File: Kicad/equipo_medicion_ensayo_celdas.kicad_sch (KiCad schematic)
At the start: 63 parts, among them J1 Conn_01x12, J3 Screw_Terminal_01x02, J4 Screw_Terminal_01x02, Q1 CSD17308Q3, Q2 CSD17308Q3, Q3 CSD17308Q3, Q4 CSD17308Q3, Q5 CSD17308Q3, Q6 2N2222A, Q7 TIP36C, U1 BQ24780SRUYR, U2 STM32WB55RGVx, U3 LM358

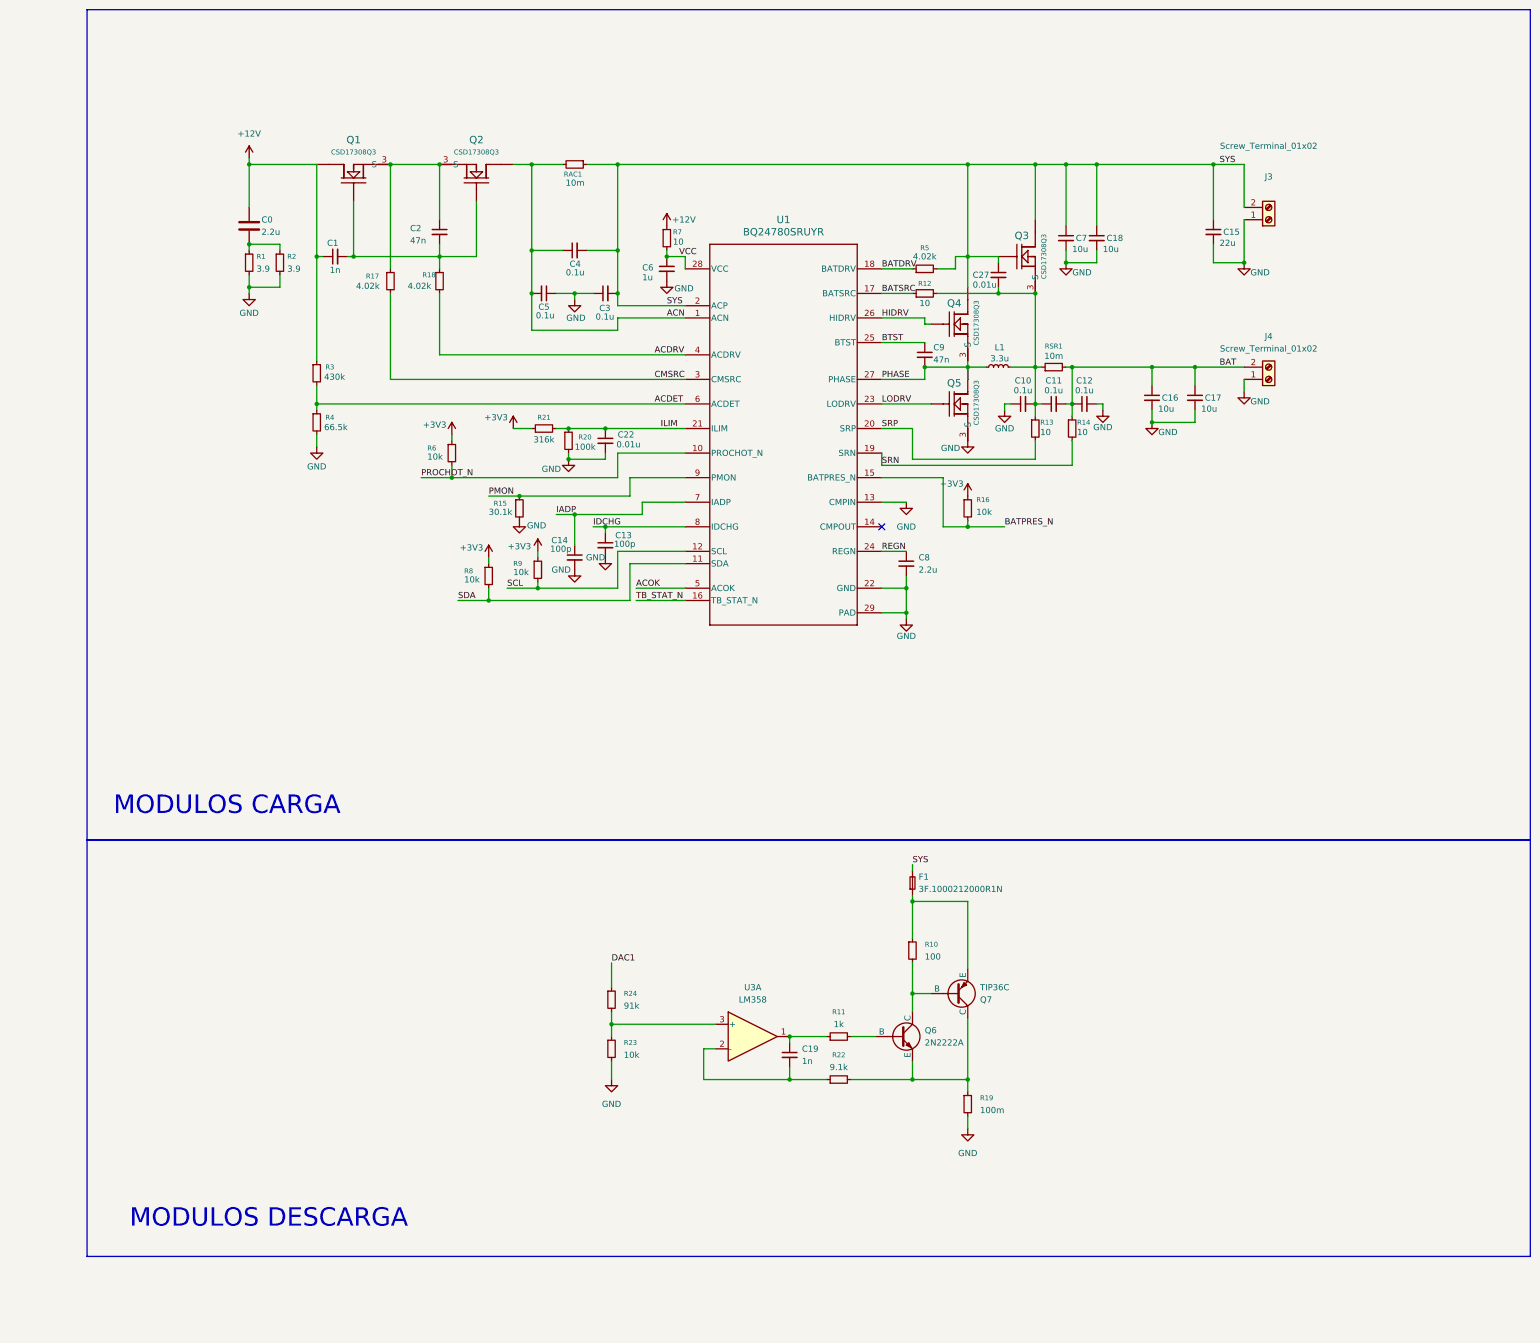
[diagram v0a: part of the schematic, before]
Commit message: Mejoras y arreglos en diseño de módulo carga/descarga/acir y fw de prueba.
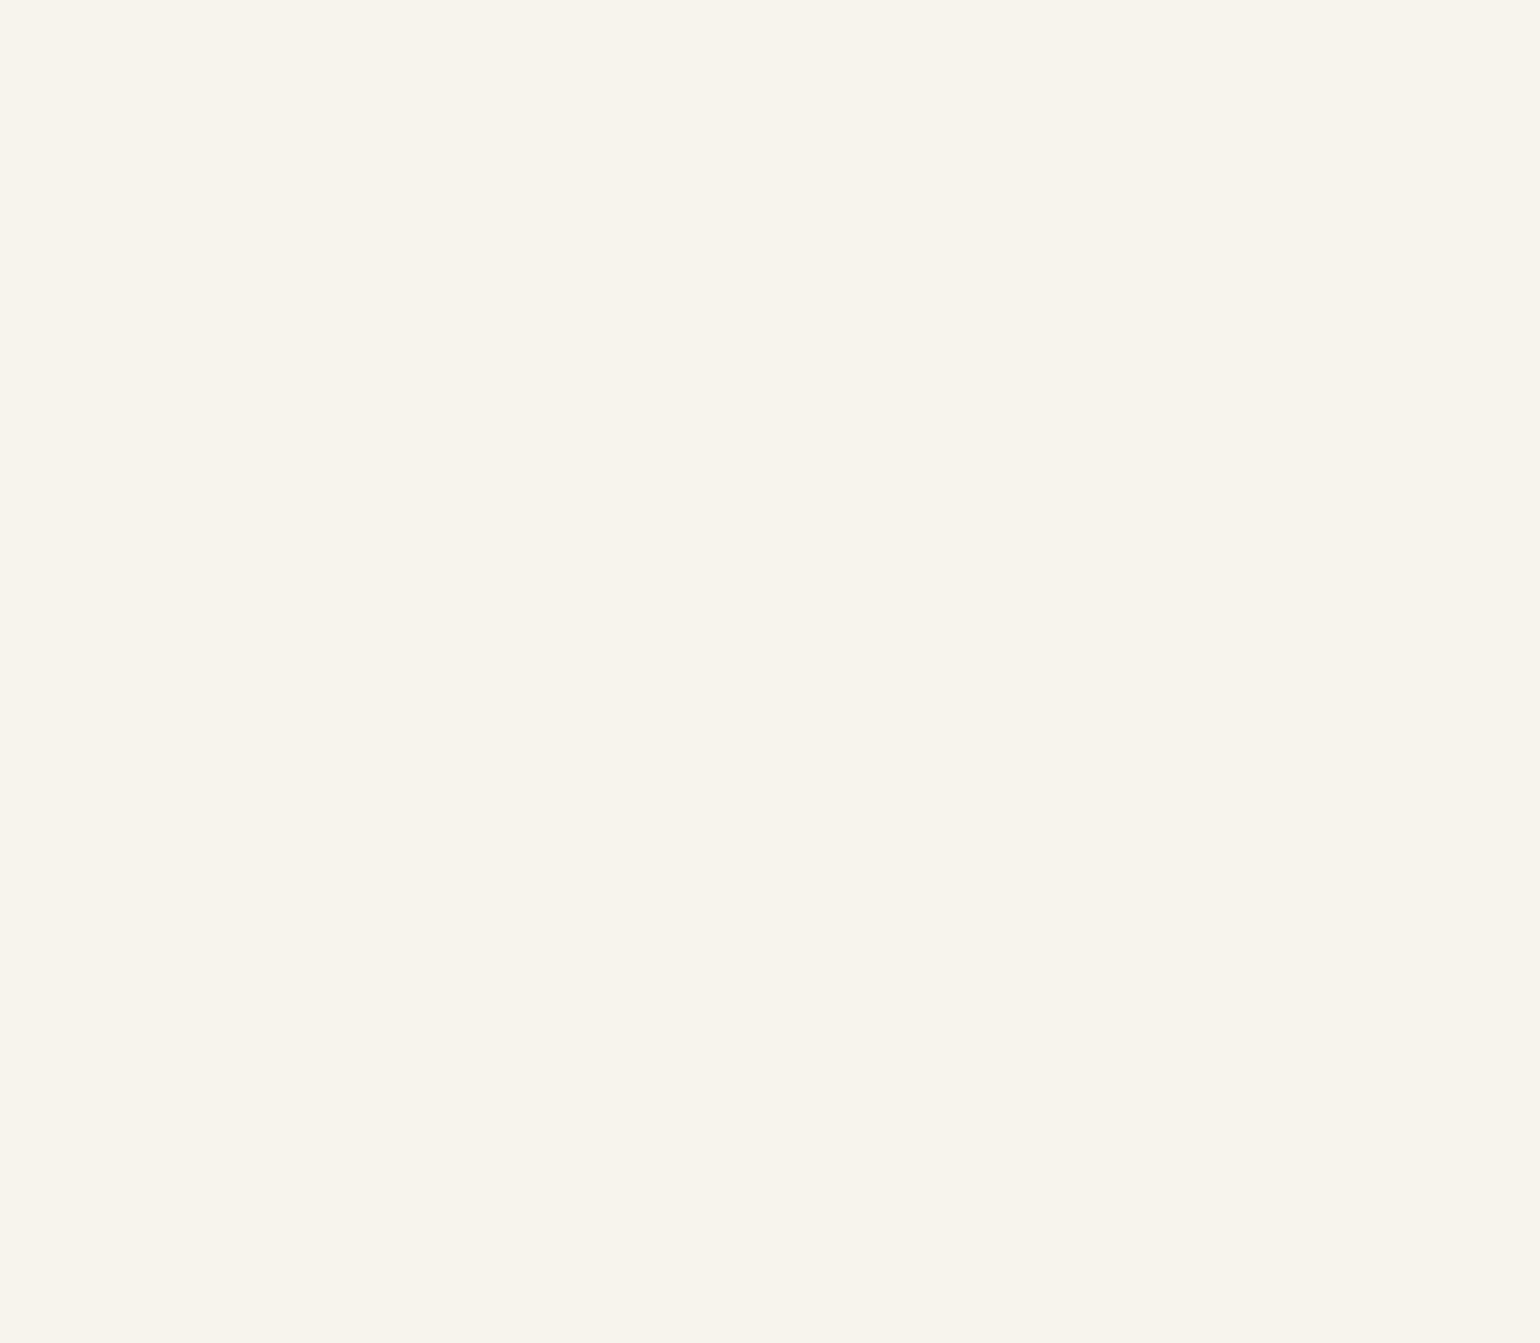
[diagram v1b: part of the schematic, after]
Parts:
- removed C0: 2.2u, Capacitor_SMD:C_0805_2012Metric, symbol Device:C
- removed C1, C19: 1n, Capacitor_SMD:C_0805_2012Metric, symbol Device:C_Small
- removed C10, C11, C12, C3, C4, C5: 0.1u, Capacitor_SMD:C_0805_2012Metric, symbol Device:C_Small
- removed C13, C14: 100p, Capacitor_SMD:C_0805_2012Metric, symbol Device:C_Small
- removed C15: 22u, Capacitor_SMD:C_0805_2012Metric, symbol Device:C_Small
- removed C16, C17, C18, C7: 10u, Capacitor_SMD:C_0805_2012Metric, symbol Device:C_Small
- removed C2, C9: 47n, Capacitor_SMD:C_0805_2012Metric, symbol Device:C_Small
- removed C22, C27: 0.01u, Capacitor_SMD:C_0805_2012Metric, symbol Device:C_Small
- removed C6: 1u, Capacitor_SMD:C_0805_2012Metric, symbol Device:C_Small
- removed C8: 2.2u, Capacitor_SMD:C_0805_2012Metric, symbol Device:C_Small
- removed F1: 3F.1000212000R1N, Fuse:Fuse_2920_7451Metric, symbol Device:Fuse_Small
- removed J3, J4: Screw_Terminal_01x02, TerminalBlock:TerminalBlock_Altech_AK300-2_P5.00mm, symbol Connector:Screw_Terminal_01x02
- removed L1: 3.3u, Inductor_THT:L_Toroid_Vertical_L16.4mm_W7.6mm_P6.60mm_Vishay_TJ3, symbol Device:L_Small
- removed Q1, Q2, Q3, Q4, Q5: CSD17308Q3, CSD17308Q3:DQG0008A, symbol CSD17308Q3:CSD17308Q3
- removed Q6: 2N2222A, Package_TO_SOT_THT:TO-92, symbol Simulation_SPICE:NPN
- removed Q7: TIP36C, Package_TO_SOT_THT:TO-247-3_Vertical, symbol Simulation_SPICE:PNP
- removed R1, R2: 3.9, Resistor_SMD:R_1206_3216Metric, symbol Device:R_Small
- removed R10: 100, Resistor_SMD:R_1206_3216Metric, symbol Device:R_Small
- removed R11: 1k, Resistor_SMD:R_1206_3216Metric, symbol Device:R_Small
- removed R12, R13, R14, R7: 10, Resistor_SMD:R_1206_3216Metric, symbol Device:R_Small
- removed R15: 30.1k, Resistor_SMD:R_1206_3216Metric, symbol Device:R_Small
- removed R16, R23, R6, R8, R9: 10k, Resistor_SMD:R_1206_3216Metric, symbol Device:R_Small
- removed R17, R18, R5: 4.02k, Resistor_SMD:R_1206_3216Metric, symbol Device:R_Small
- removed R19: 100m, Resistor_SMD:R_1206_3216Metric, symbol Device:R_Small
- removed R20: 100k, Resistor_SMD:R_1206_3216Metric, symbol Device:R_Small
- removed R21: 316k, Resistor_SMD:R_1206_3216Metric, symbol Device:R_Small
- removed R22: 9.1k, Resistor_SMD:R_1206_3216Metric, symbol Device:R_Small
- removed R24: 91k, Resistor_SMD:R_1206_3216Metric, symbol Device:R_Small
- removed R3: 430k, Resistor_SMD:R_1206_3216Metric, symbol Device:R_Small
- removed R4: 66.5k, Resistor_SMD:R_1206_3216Metric, symbol Device:R_Small
- removed RAC1, RSR1: 10m, Resistor_SMD:R_1206_3216Metric, symbol Device:R_Small
- removed U1: BQ24780SRUYR, BQ24780S:RUY0028A, symbol project_sch_symbols:BQ24780SRUYR
- removed U3: LM358, Package_SO:SOIC-8-1EP_3.9x4.9mm_P1.27mm_EP2.29x3mm, symbol Amplifier_Operational:LM358
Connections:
- no-connect marks 1 -> 0
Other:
- note removed: "MODULOS CARGA"
- note removed: "MODULOS DESCARGA"

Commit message: Más avances en esquemático de Kicad.
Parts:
- added C1, C10, C2, C3, C4, C5, C6, C9: 100n, symbol Device:C
- added C11, C12: C, symbol Device:C
- added C13: 0p8, symbol Device:C
- added C14: 0p3, symbol Device:C
- added C7, C8: 4u7, symbol Device:C
- added FLT1: DLF162500LT-5028A1, equipo_medicion_ensayo_celdas_footprints:DLF162500LT-5028A1, symbol equipo_medicion_ensayo_celdas_sch_symbols:DLF162500LT-5028A1
- added J2: Conn_Coaxial, symbol Connector:Conn_Coaxial
- added L1: 2n7, symbol Device:L
- added X1: 32.768kHz, symbol Device:Crystal
- added X2: 32MHz, symbol Device:Crystal_GND24_Small
- renumbered U2 to U1
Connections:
- net +3V3: now also U1.1 (VBAT), U1.14 (VDDA), U1.30 (VDD), U1.33 (VDDRF), U1.41 (VFBSMPS), U1.43 (VLXSMPS), U1.44 (VDDSMPS), U1.45 (VDD), U1.55 (VDDUSB), U1.68 (VDD), C1.1, C10.1, C2.1, C3.1, C4.1, C5.1, C6.1, C7.1, C8.1, C9.1
- net GND: now also U1.32 (VSSRF), U1.42 (VSSSMPS), U1.69 (VSS), C1.2, C10.2, C11.2, C12.2, C13.2, C14.2, C2.2, C3.2, C4.2, C5.2, C6.2, C7.2, C8.2, C9.2, FLT1.2 (GND), FLT1.4 (GND), J2.2 (Ext), X2.2, X2.4
- net LSE_IN: now reaches U1.3 (PC14)
- net LSE_IN: now also C12.1, X1.2
- net RF: now reaches U1.31 (RF1)
- net RF: now also C13.1, L1.1
- net HSE_OUT: now reaches U1.34 (OSC_OUT)
- net HSE_OUT: now also X2.3
- net HSE_IN: now reaches U1.35 (OSC_IN)
- net HSE_IN: now also X2.1
- net LSE_OUT: now reaches U1.4 (PC15)
- net LSE_OUT: now also C11.1, X1.1
- new net RF_ANT: FLT1.3 (OUT), J2.1 (In)
- new net RF_MATCH: C14.1, FLT1.1 (IN), L1.2
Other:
- moved on the sheet: U1

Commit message: Correcciones en simulaciones y avances en el esquemático.
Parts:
- removed J1: Conn_01x12, Connector_PinHeader_2.54mm:PinHeader_1x12_P2.54mm_Vertical, symbol Connector_Generic:Conn_01x12
- added C15, C16: 100n, symbol Device:C
- added D1: LED, symbol Device:LED
- added J3: Conn_01x06, Connector_PinHeader_2.54mm:PinHeader_1x06_P2.54mm_Vertical, symbol Connector_Generic:Conn_01x06
- added J4: USB_C_Receptacle_USB2.0_16P, symbol Connector:USB_C_Receptacle_USB2.0_16P
- added R1, R3, R4: 5K1, symbol Device:R
- added R2, R6: 220, symbol Device:R
- added SW1, SW2: SW_Push, symbol Switch:SW_Push
- added U2: USBLC6-2SC6, Package_TO_SOT_SMD:SOT-23-6, symbol Power_Protection:USBLC6-2SC6
- added U3: TPS54560BQDDAQ1, Package_SO:Texas_R-PDSO-G8_EP2.95x4.9mm_Mask2.4x3.1mm, symbol equipo_medicion_ensayo_celdas_sch_symbols:TPS54560BQDDAQ1
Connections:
- net +3V3: now also J3.1 (Pin_1), SW2.2
- net GND: now also C15.2, C16.2, J3.6 (Pin_6), J4.A1 (GND), J4.A12 (GND), J4.B1 (GND), J4.B12 (GND), J4.S1 (SHIELD), R1.2, R3.2, R4.2, R6.1, SW1.2, U2.2 (GND)
- net at U1.22 (PA7): now also D1.2 (A)
- net BOOT0: now reaches U1.5 (PH3)
- net BOOT0: now also C16.1, R1.1, R2.1
- net USB_D-: now reaches U1.52 (PA11)
- net USB_D-: now also U2.6 (I/O1)
- net USB_D+: now reaches U1.53 (PA12)
- net USB_D+: now also U2.4 (I/O2)
- net SWDIO: now reaches U1.54 (PA13)
- net SWDIO: now also J3.4 (Pin_4)
- net SWCLK: now reaches U1.56 (PA14)
- net SWCLK: now also J3.3 (Pin_3)
- net SWO: now reaches U1.63 (PB3)
- net SWO: now also J3.5 (Pin_5)
- net SWD_NRST: now reaches U1.8 (NRST)
- net SWD_NRST: now also C15.1, J3.2 (Pin_2), SW1.1
- new net: J4.A7 (D-), J4.B7 (D-), U2.1 (I/O1)
- new net: J4.A6 (D+), J4.B6 (D+), U2.3 (I/O2)
- new net: J4.A4 (VBUS), J4.A9 (VBUS), J4.B4 (VBUS), J4.B9 (VBUS), U2.5 (VBUS)
- new net: R2.2, SW2.1
- new net: J4.A5 (CC1), R4.1
- new net: J4.B5 (CC2), R3.1
- new net LED_K: D1.1 (K), R6.2
- no-connect marks 0 -> 4
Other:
- moved on the sheet: C1, C10, C11, C12, C13, C14, C2, C3, C4, C5, C6, C7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

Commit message: Más avances en la parte de alimentación (POWER IN) del esquemático.
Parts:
- removed U3: TPS54560BQDDAQ1, Package_SO:Texas_R-PDSO-G8_EP2.95x4.9mm_Mask2.4x3.1mm, symbol equipo_medicion_ensayo_celdas_sch_symbols:TPS54560BQDDAQ1
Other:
- added sheet POWER_IN (eq_med_celdas_power_in.kicad_sch)
